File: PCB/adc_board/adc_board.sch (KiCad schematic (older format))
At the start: 18 parts, among them J1 Conn_02x05_Counter_Clockwise, U1 MCP1755T-3302E_OT, U2 MAX6070BAUT33T

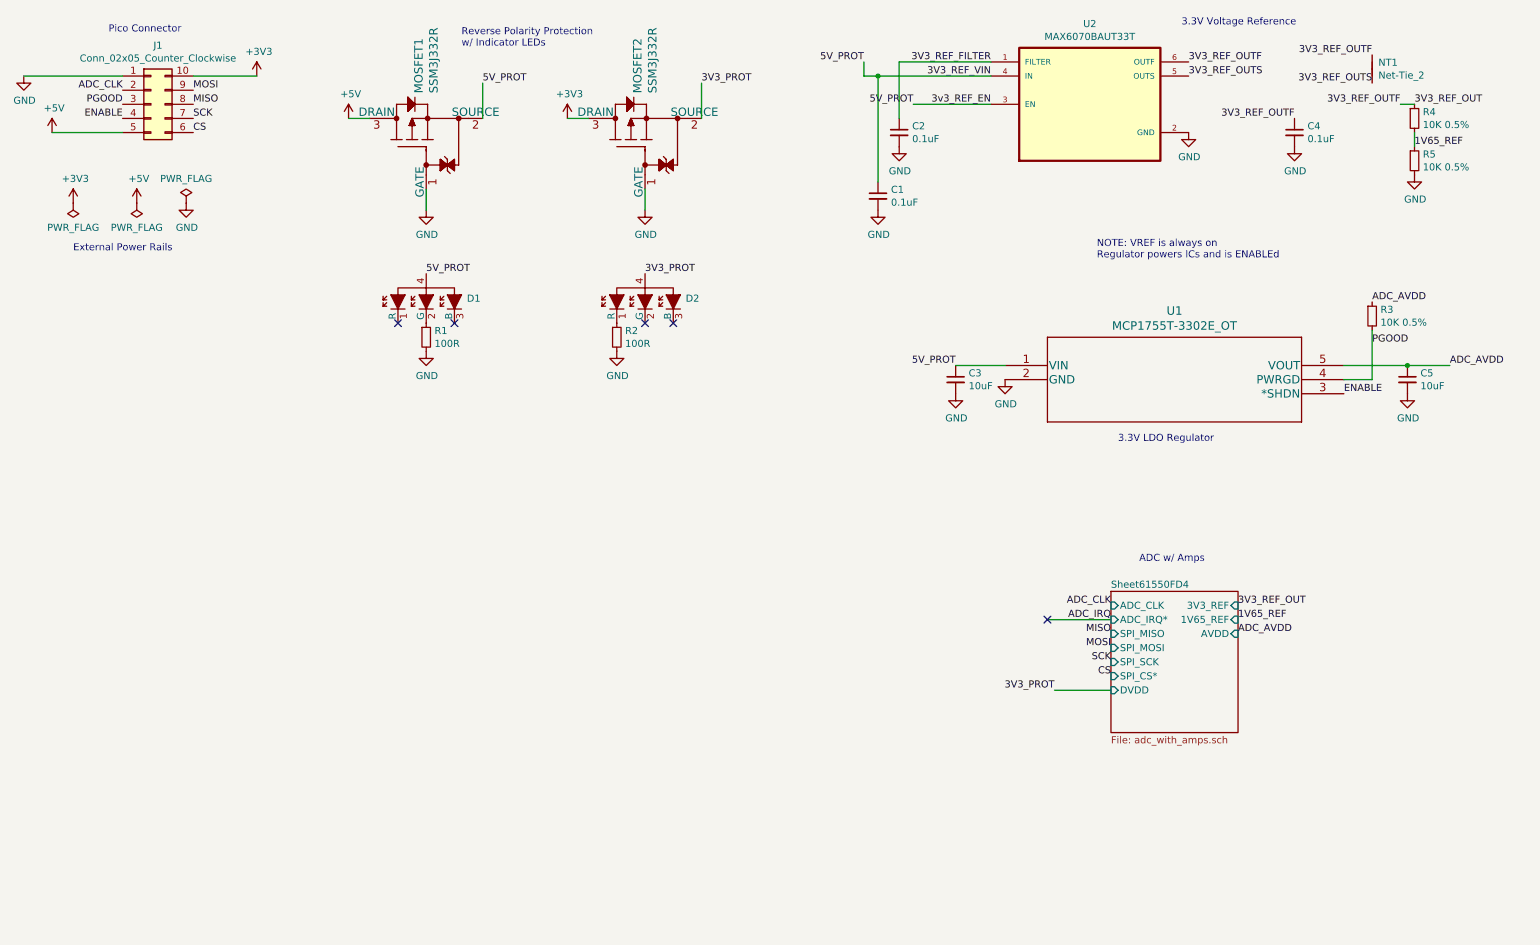
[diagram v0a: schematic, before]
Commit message: Finished layout for adc board
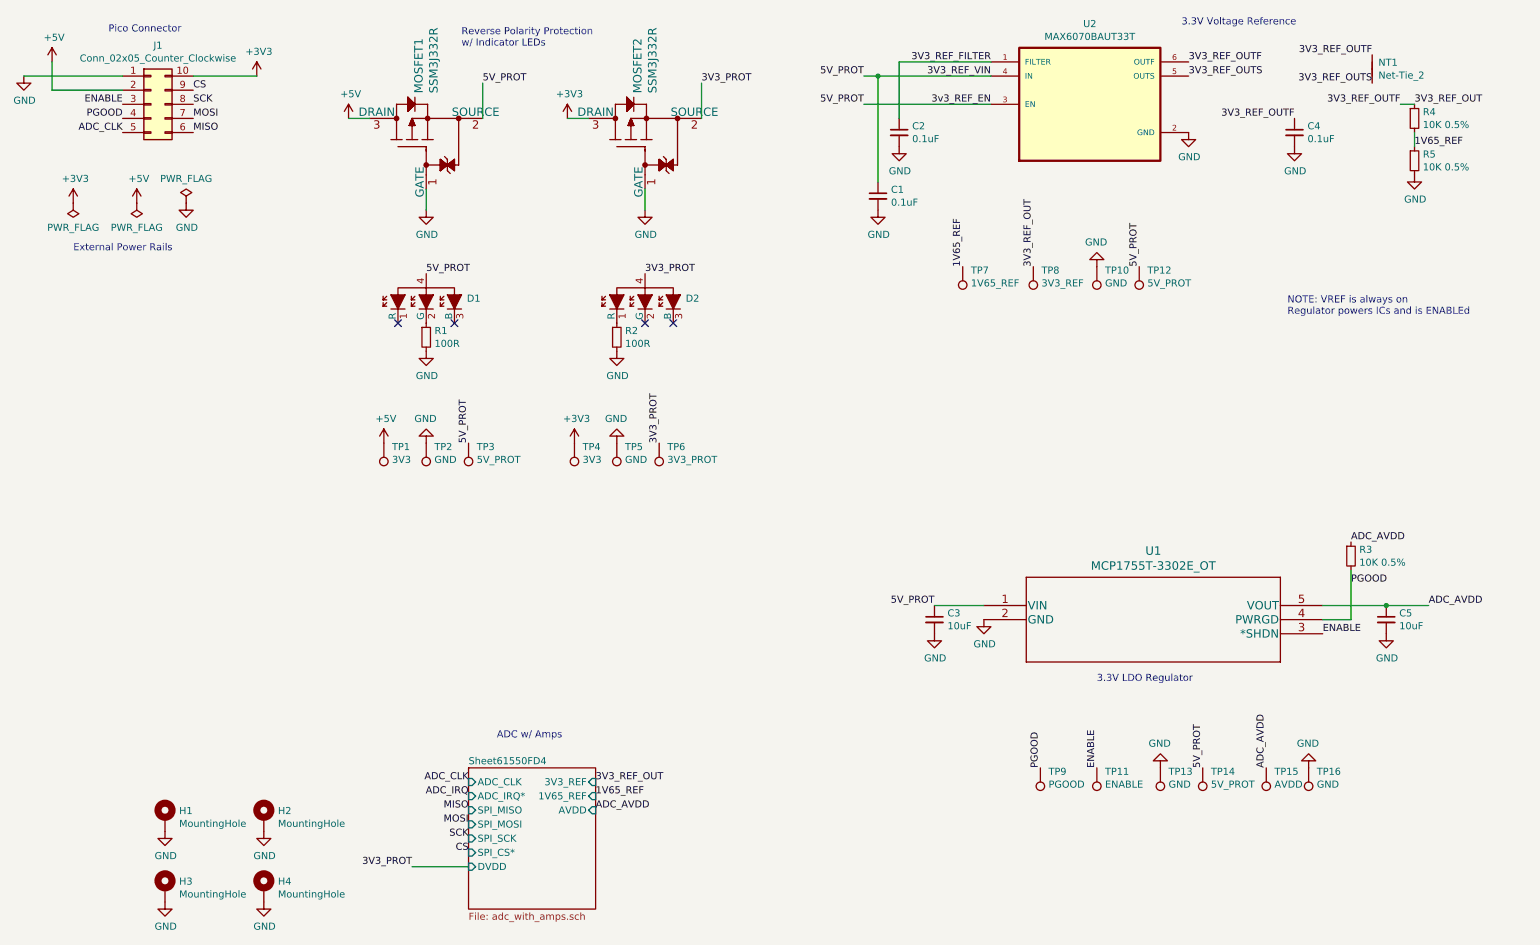
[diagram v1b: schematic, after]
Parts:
- added H1, H2, H3, H4: MountingHole, MountingHole:MountingHole_3.2mm_M3_Pad_Via, symbol Mechanical:MountingHole_Pad
- added TP1, TP4: 3V3, TestPoint:TestPoint_Pad_D1.0mm, symbol Connector:TestPoint
- added TP10, TP13, TP16, TP2, TP5: GND, TestPoint:TestPoint_Pad_D1.0mm, symbol Connector:TestPoint
- added TP11: ENABLE, TestPoint:TestPoint_Pad_D1.0mm, symbol Connector:TestPoint
- added TP12, TP14, TP3: 5V_PROT, TestPoint:TestPoint_Pad_D1.0mm, symbol Connector:TestPoint
- added TP15: AVDD, TestPoint:TestPoint_Pad_D1.0mm, symbol Connector:TestPoint
- added TP6: 3V3_PROT, TestPoint:TestPoint_Pad_D1.0mm, symbol Connector:TestPoint
- added TP7: 1V65_REF, TestPoint:TestPoint_Pad_D1.0mm, symbol Connector:TestPoint
- added TP8: 3V3_REF, TestPoint:TestPoint_Pad_D1.0mm, symbol Connector:TestPoint
- added TP9: PGOOD, TestPoint:TestPoint_Pad_D1.0mm, symbol Connector:TestPoint
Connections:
- net +3V3: now also TP4.1
- net +5V: now also J1.2 (Pin_2), TP1.1; no longer J1.5 (Pin_5)
- net 1V65_REF: now also TP7.1
- net 3V3_PROT: now also TP6.1
- net 3V3_REF_OUT: now also TP8.1
- net 3V3_REF_VIN: now also TP12.1, TP14.1, TP3.1
- net ADC_AVDD: now also TP15.1
- net ADC_CLK: now also J1.5 (Pin_5); no longer J1.2 (Pin_2)
- net CS: now also J1.9 (Pin_9); no longer J1.6 (Pin_6)
- net ENABLE: now also J1.3 (Pin_3), TP11.1; no longer J1.4 (Pin_4)
- net GND: now also H1.1, H2.1, H3.1, H4.1, TP10.1, TP13.1, TP16.1, TP2.1, TP5.1
- net MISO: now also J1.6 (Pin_6); no longer J1.8 (Pin_8)
- net MOSI: now also J1.7 (Pin_7); no longer J1.9 (Pin_9)
- net PGOOD: now also J1.4 (Pin_4), TP9.1; no longer J1.3 (Pin_3)
- net SCK: now also J1.8 (Pin_8); no longer J1.7 (Pin_7)
- no-connect marks 5 -> 4
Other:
- moved on the sheet: C3, C5, R3, U1
